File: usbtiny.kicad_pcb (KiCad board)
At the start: 2 copper layers, 19 parts, among them IC1 ATTINY2313-P, P2 USB_A, P3 CONN_01X06, Y1 12MHz

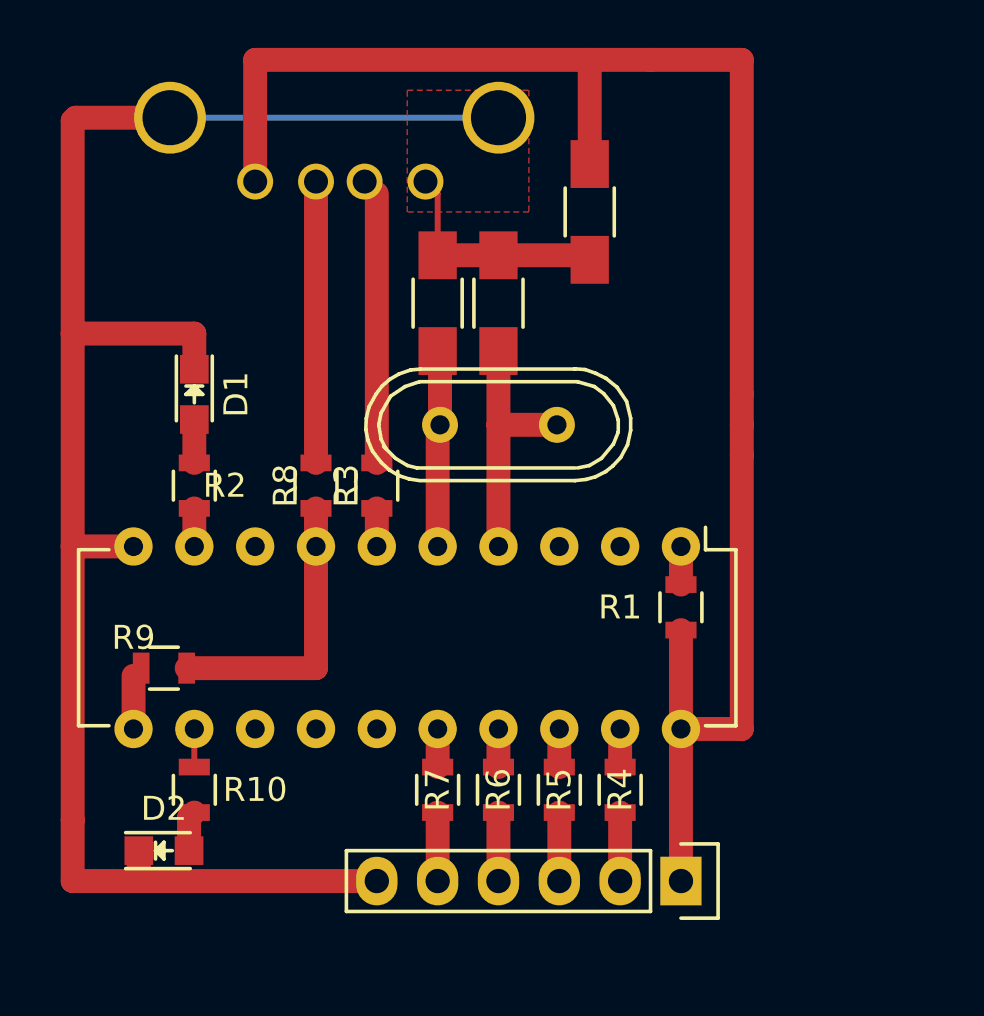
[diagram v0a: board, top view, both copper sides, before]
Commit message: Reduced the PCB size
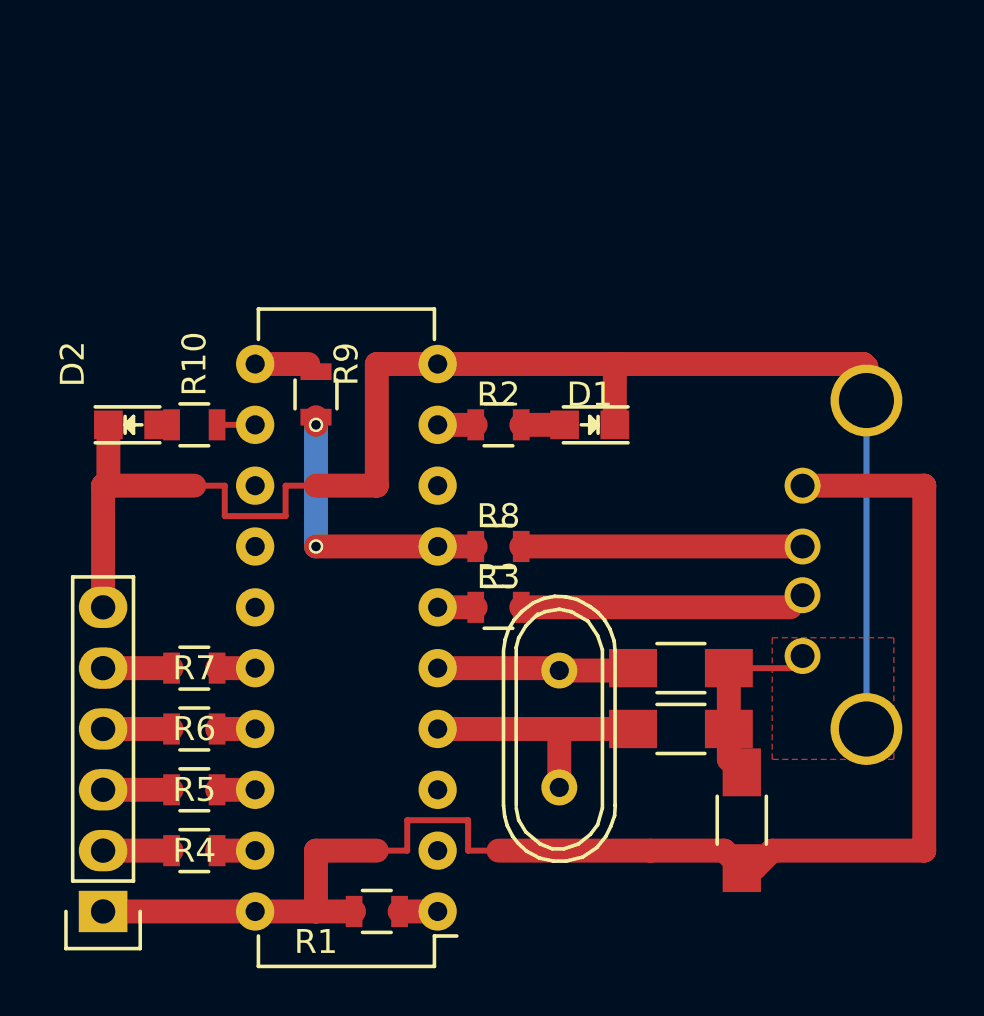
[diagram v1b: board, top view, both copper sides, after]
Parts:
- IC1: value ATTINY2313-P -> ATTINY2313
- moved C3 26.2 mm to (205.7, 92.7), turned to 90 degrees
- moved P2 26.2 mm to (208.3, 78.7), turned to 270 degrees
- moved P3 24.2 mm to (179.1, 96.5), turned to 180 degrees
- moved C1 19.3 mm to (203.2, 88.9), turned to 180 degrees
- moved C2 18.3 mm to (203.2, 86.4), turned to 0 degrees
- moved IC1 18.3 mm to (193.0, 96.5), turned to 180 degrees
- moved R4 18.0 mm to (182.9, 94.0), turned to 180 degrees
- moved R1 18.0 mm to (190.5, 96.5), turned to 0 degrees
- moved D2 17.8 mm to (180.3, 76.2)
- moved D1 16.6 mm to (199.4, 76.2), turned to 180 degrees
- moved R5 15.2 mm to (182.9, 91.4), turned to 180 degrees
- moved R10 15.2 mm to (182.9, 76.2), turned to 180 degrees
- moved R9 13.1 mm to (188.0, 74.9), turned to 90 degrees
- moved R2 13.0 mm to (195.6, 76.2), turned to 0 degrees
- moved R6 13.0 mm to (182.9, 88.9), turned to 180 degrees
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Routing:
- net GNDREF: track 83.7 -> 74.3 mm
- net VCC: track 71.0 -> 62.2 mm
- net Net-(D2-Pad2): track 1.75 -> 0.00 mm
- net Net-(IC1-Pad7): vias 0 -> 2
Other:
- board text added: "Bend pin13 so it does not go through hole. Then you can connect this strait."
- board text added: "Bend pin2 so it does not go through hole. Then you can connect this strait."
